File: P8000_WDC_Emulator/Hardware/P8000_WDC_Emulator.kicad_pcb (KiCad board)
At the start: 2 copper layers, 144 x 160.4 mm, 92 parts, among them Q1 CRYSTAL, SW1 SW_PUSH, X1 RS-232, X2 P8000, X3 SD-CON, X4 PATA, X5 4_Pin_Molex, X6 P8000-Compact, X7 AVR-ISP-6

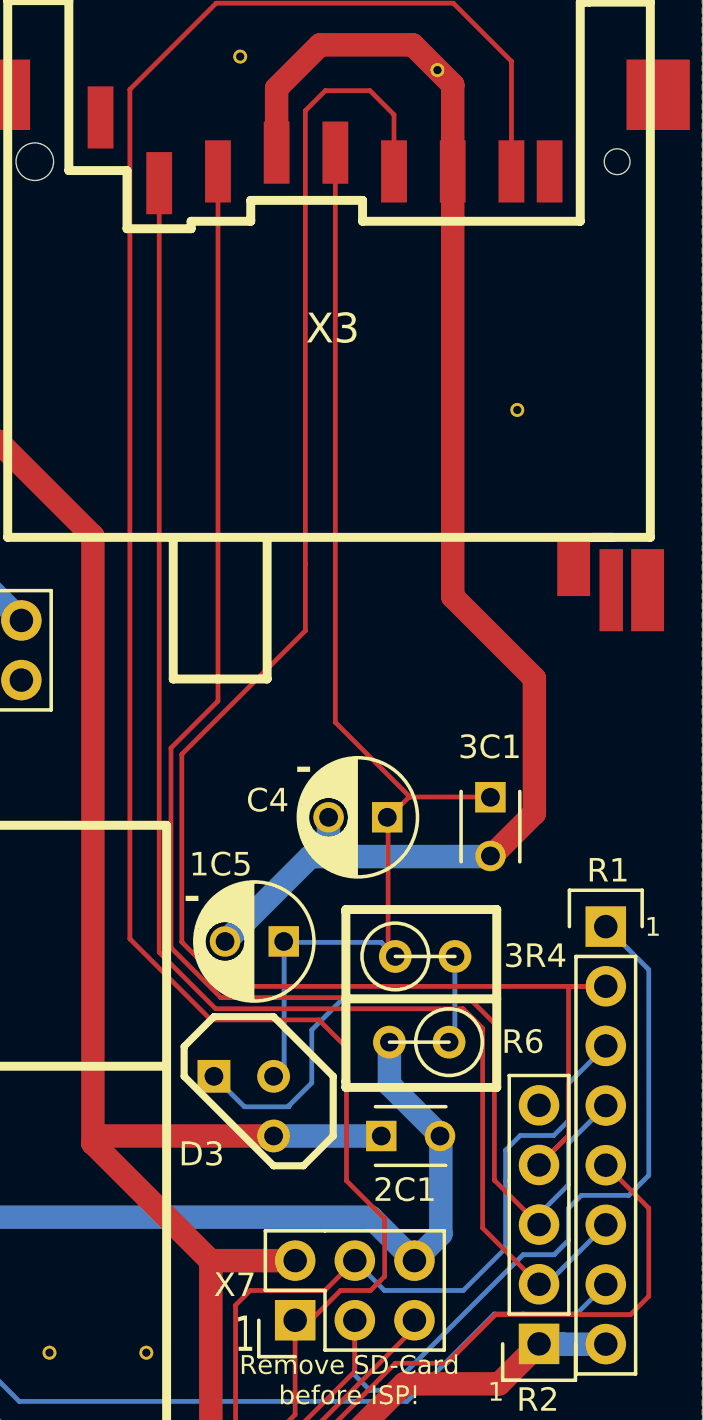
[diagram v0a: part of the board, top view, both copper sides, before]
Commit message: power line sizes for 3.3V
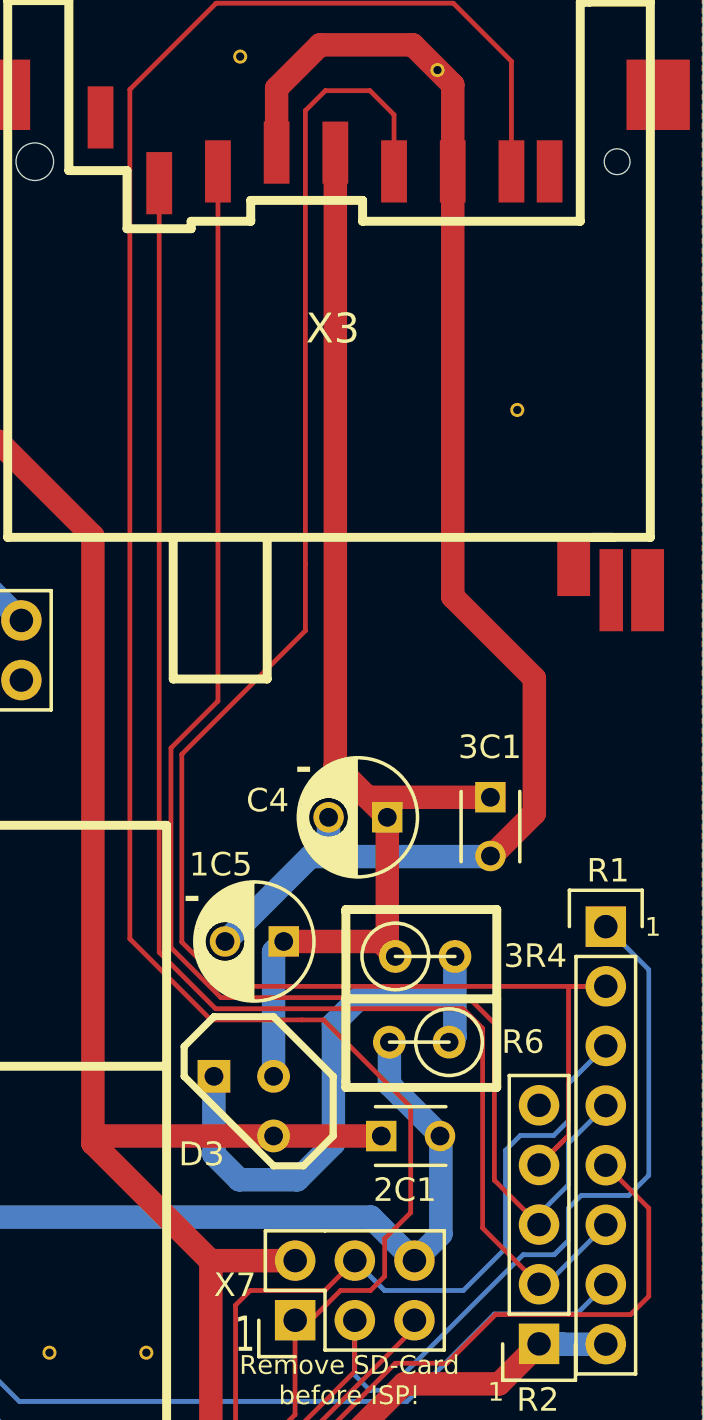
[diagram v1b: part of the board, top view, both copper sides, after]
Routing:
- net Net-(3R4-Pad2): track 17.8 -> 24.0 mm
- net +3V3: track 50.4 -> 53.4 mm
- net Net-(D1-Pad7): track 128.9 -> 129.9 mm
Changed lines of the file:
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@@
     (thickness 1.6002)
     (drawings 45)
-    (tracks 1224)
+    (tracks 1225)
     (zones 0)
     (modules 92)
@@
     (uvia_dia 0.508)
     (uvia_drill 0.127)
-    (add_net +3V3)
     (add_net //ASTB)
     (add_net //CS0)
@@
     (add_net "Net-(3C5-Pad1)")
     (add_net "Net-(3C5-Pad2)")
-    (add_net "Net-(3R4-Pad2)")
     (add_net "Net-(4C5-Pad2)")
     (add_net "Net-(5C5-Pad1)")
@@
     (uvia_dia 0.508)
     (uvia_drill 0.127)
+    (add_net +3V3)
     (add_net GND)
+    (add_net "Net-(3R4-Pad2)")
     (add_net VCC)
   )
@@
   (segment (start 146.32432 164.8206) (end 147.04568 164.09924) (width 1.00076) (layer Front) (net 41))
   (segment (start 146.32432 177.90414) (end 146.32432 164.8206) (width 1.00076) (layer Front) (net 41))
+  (segment (start 145.17116 74.39406) (end 149.75586 74.39406) (width 1.00076) (layer Front) (net 42))
+  (segment (start 149.75586 74.39406) (end 149.7584 74.3966) (width 1.00076) (layer Front) (net 42))
   (segment (start 149.75078 74.39406) (end 149.75586 74.39914) (width 1.00076) (layer Back) (net 42))
   (segment (start 66.04508 40.3606) (end 70.17512 36.23056) (width 1.00076) (layer Front) (net 42))
@@
   (segment (start 137.7823 74.39406) (end 137.47496 74.7014) (width 1.00076) (layer Front) (net 42))
   (segment (start 66.04508 41.28516) (end 75.77582 51.0159) (width 1.00076) (layer Front) (net 42))
-  (segment (start 145.17116 74.39406) (end 149.75078 74.39406) (width 1.00076) (layer Back) (net 42))
   (segment (start 75.77582 51.0159) (end 75.77582 59.25566) (width 1.00076) (layer Front) (net 42))
   (segment (start 145.17116 74.39406) (end 137.7823 74.39406) (width 1.00076) (layer Front) (net 42))
@@
   (segment (start 29.47416 115.12296) (end 29.47416 114.21364) (width 0.2032) (layer Back) (net 43))
   (segment (start 145.10004 95.60052) (end 152.67432 103.1748) (width 0.2032) (layer Front) (net 43))
-  (segment (start 150.04796 66.44132) (end 150.3553 66.74866) (width 0.2032) (layer Front) (net 44))
-  (segment (start 149.75586 66.14922) (end 150.3553 66.74866) (width 0.2032) (layer Back) (net 44))
-  (segment (start 145.62074 66.14922) (end 149.75586 66.14922) (width 0.2032) (layer Back) (net 44))
-  (segment (start 147.80006 32.51454) (end 147.80006 56.77662) (width 0.2032) (layer Front) (net 44))
-  (segment (start 147.80006 56.77662) (end 150.98014 59.9567) (width 0.2032) (layer Front) (net 44))
-  (segment (start 150.98014 59.9567) (end 150.94204 59.9567) (width 0.2032) (layer Front) (net 44))
-  (segment (start 150.94204 59.9567) (end 150.04796 60.85078) (width 0.2032) (layer Front) (net 44))
-  (segment (start 145.62074 71.40448) (end 145.17116 71.85406) (width 0.2032) (layer Back) (net 44))
-  (segment (start 145.62074 66.14922) (end 145.62074 71.40448) (width 0.2032) (layer Back) (net 44))
-  (segment (start 154.42946 59.9567) (end 150.98014 59.9567) (width 0.2032) (layer Front) (net 44))
-  (segment (start 150.04796 60.85078) (end 150.04796 66.44132) (width 0.2032) (layer Front) (net 44))
+  (segment (start 145.17116 71.85406) (end 145.17116 66.54292) (width 1.00076) (layer Back) (net 44))
+  (segment (start 145.17116 66.54292) (end 145.60296 66.11112) (width 1.00076) (layer Back) (net 44))
+  (segment (start 145.60296 66.11112) (end 149.71776 66.11112) (width 1.00076) (layer Front) (net 44))
+  (segment (start 149.71776 66.11112) (end 150.3553 66.74866) (width 1.00076) (layer Front) (net 44))
+  (segment (start 150.0124 60.82284) (end 150.0124 66.40576) (width 1.00076) (layer Front) (net 44))
+  (segment (start 150.0124 66.40576) (end 150.3553 66.74866) (width 1.00076) (layer Front) (net 44))
+  (segment (start 154.4066 59.9694) (end 149.15896 59.9694) (width 1.00076) (layer Front) (net 44))
+  (segment (start 149.15896 59.9694) (end 147.80006 58.6105) (width 1.00076) (layer Front) (net 44))
+  (segment (start 147.80006 32.51454) (end 147.80006 58.6105) (width 1.00076) (layer Front) (net 44))
+  (segment (start 147.80006 58.6105) (end 149.04 59.85044) (width 1.00076) (layer Front) (net 44))
+  (segment (start 149.04 59.85044) (end 150.0124 60.82284) (width 1.00076) (layer Front) (net 44))
   (segment (start 103.4 39.40048) (end 103.01224 39.40048) (width 0.2032) (layer Back) (net 45))
   (segment (start 103.01224 39.40048) (end 102.25272 40.16) (width 0.2032) (layer Back) (net 45))
@@
   (segment (start 30.06598 54.7497) (end 29.718 55.09768) (width 0.2032) (layer Back) (net 56))
   (segment (start 29.718 55.09768) (end 25.82672 55.09768) (width 0.2032) (layer Back) (net 56))
-  (segment (start 146.7993 72.12584) (end 146.7993 69.8754) (width 0.2032) (layer Back) (net 57))
-  (segment (start 152.8953 70.14718) (end 152.64384 70.39864) (width 0.2032) (layer Back) (net 57))
-  (segment (start 152.8953 68.60032) (end 151.74976 68.60032) (width 0.2032) (layer Back) (net 57))
-  (segment (start 145.82648 73.14946) (end 145.82648 73.09866) (width 0.2032) (layer Back) (net 57))
-  (segment (start 152.8953 66.74866) (end 152.8953 68.60032) (width 0.2032) (layer Back) (net 57))
-  (segment (start 148.07438 68.60032) (end 151.74976 68.60032) (width 0.2032) (layer Back) (net 57))
-  (segment (start 145.82648 73.09866) (end 146.7993 72.12584) (width 0.2032) (layer Back) (net 57))
-  (segment (start 143.92656 73.14946) (end 145.82648 73.14946) (width 0.2032) (layer Back) (net 57))
-  (segment (start 152.8953 68.60032) (end 152.8953 70.14718) (width 0.2032) (layer Back) (net 57))
-  (segment (start 146.7993 69.8754) (end 148.07438 68.60032) (width 0.2032) (layer Back) (net 57))
-  (segment (start 143.92656 73.14946) (end 142.63116 71.85406) (width 0.2032) (layer Back) (net 57))
+  (segment (start 152.8953 68.56) (end 148.78 68.56) (width 1.00076) (layer Back) (net 57))
+  (segment (start 142.63116 75.18116) (end 142.63116 71.85406) (width 1.00076) (layer Back) (net 57))
+  (segment (start 143.71 76.26) (end 142.63116 75.18116) (width 1.00076) (layer Back) (net 57))
+  (segment (start 146.18 76.26) (end 143.71 76.26) (width 1.00076) (layer Back) (net 57))
+  (segment (start 147.72 74.72) (end 146.18 76.26) (width 1.00076) (layer Back) (net 57))
+  (segment (start 147.72 69.62) (end 147.72 74.72) (width 1.00076) (layer Back) (net 57))
+  (segment (start 148.78 68.56) (end 147.72 69.62) (width 1.00076) (layer Back) (net 57))
+  (segment (start 152.8953 66.74866) (end 152.8953 68.56) (width 1.00076) (layer Back) (net 57))
+  (segment (start 152.8953 68.56) (end 152.8953 70.14718) (width 1.00076) (layer Back) (net 57))
+  (segment (start 152.8953 70.14718) (end 152.64384 70.39864) (width 1.00076) (layer Back) (net 57))
   (segment (start 30.06598 62.3697) (end 26.3144 66.12128) (width 0.2032) (layer Back) (net 58))
   (segment (start 26.3144 66.12128) (end 25.84958 66.12128) (width 0.2032) (layer Back) (net 58))
@@
   (segment (start 155.6766 74.37374) (end 155.04922 75.00112) (width 0.2032) (layer Back) (net 61))
   (segment (start 157.10154 74.37374) (end 155.6766 74.37374) (width 0.2032) (layer Back) (net 61))
-  (segment (start 148.27504 70.6247) (end 148.27504 76.3016) (width 0.2032) (layer Front) (net 62))
-  (segment (start 147.10156 69.45122) (end 148.27504 70.6247) (width 0.2032) (layer Front) (net 62))
-  (segment (start 142.50162 69.45122) (end 147.10156 69.45122) (width 0.2032) (layer Front) (net 62))
+  (segment (start 146.38 69.45122) (end 147.30122 69.45122) (width 0.2032) (layer Front) (net 62))
+  (segment (start 151.01 77.66) (end 149.90064 78.76936) (width 0.2032) (layer Front) (net 62))
+  (segment (start 151.01 73.16) (end 151.01 77.66) (width 0.2032) (layer Front) (net 62))
+  (segment (start 147.30122 69.45122) (end 151.01 73.16) (width 0.2032) (layer Front) (net 62))
+  (segment (start 142.50162 69.45122) (end 146.38 69.45122) (width 0.2032) (layer Front) (net 62))
   (segment (start 148.02358 80.9752) (end 146.75358 82.2452) (width 0.2032) (layer Front) (net 62))
   (segment (start 149.29866 80.9752) (end 148.02358 80.9752) (width 0.2032) (layer Front) (net 62))
   (segment (start 149.90064 80.37322) (end 149.29866 80.9752) (width 0.2032) (layer Front) (net 62))
-  (segment (start 149.90064 77.9272) (end 149.90064 80.37322) (width 0.2032) (layer Front) (net 62))
-  (segment (start 148.27504 76.3016) (end 149.90064 77.9272) (width 0.2032) (layer Front) (net 62))
+  (segment (start 149.90064 78.76936) (end 149.90064 80.37322) (width 0.2032) (layer Front) (net 62))
   (segment (start 144.05102 92.49918) (end 144.05102 95.9993) (width 0.2032) (layer Front) (net 62))
   (segment (start 151.6761 112.9411) (end 145.7452 118.872) (width 0.2032) (layer Front) (net 62))

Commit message: begin work on v2.1
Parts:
- removed 1C5: 1u, Capacitors_ThroughHole:C_Radial_D5_L6_P2.5
- removed 1D5, 2D5: 74HCT245, Housings_DIP:DIP-20_W7.62mm
- removed 1R5, 2R5: 4k7, Pin_Headers:Pin_Header_Straight_1x05
- removed 3R4: 220, Discret:R1
- removed C4: 47u, Capacitors_ThroughHole:C_Radial_D5_L6_P2.5
- removed R6: 330, Discret:R1
- added 1C3: 100u, Capacitors_ThroughHole:C_Radial_D5_L6_P2.5, F.Cu at (199.1, 82.6)
- added 1C4: 1u, Capacitors_ThroughHole:C_Radial_D5_L6_P2.5, F.Cu at (3.75, 40.0)
- added 2C3: 100u, Capacitors_ThroughHole:C_Radial_D5_L6_P2.5, F.Cu at (213.1, 82.0)
- added 2C4: 1u, Capacitors_ThroughHole:C_Radial_D5_L6_P2.5, F.Cu at (-17.2, 41.4)
- added 3C4: 1u, Capacitors_ThroughHole:C_Radial_D5_L6_P2.5, F.Cu at (-6.99, 44.3)
- added 4C4: 1u, Capacitors_ThroughHole:C_Radial_D5_L6_P2.5, F.Cu at (-31.1, 44.7)
- added 7C1: 100n, Capacitors_ThroughHole:C_Disc_D3_P2.5, F.Cu at (175.8, 146.8)
- added 8C1: 100n, Capacitors_ThroughHole:C_Disc_D3_P2.5, F.Cu at (171.0, 139.5)
- added C2: 470u, Capacitors_ThroughHole:C_Radial_D5_L6_P2.5, F.Cu at (3.68, 27.8)
- added D5: 74HCT245, Housings_DIP:DIP-20_W7.62mm, F.Cu at (97.2, 33.7)
- added D6: 74HCT243, Housings_DIP:DIP-14_W7.62mm, F.Cu at (125.0, 42.0)
- added D7: 74HCT573, Housings_DIP:DIP-20_W7.62mm, F.Cu at (128.7, 31.8)
- D3: value LM317 -> TS1117 BCW33; footprint TO92-LM317 -> TO_SOT_Packages_SMD:SOT-223
- D4: value 74HCT03 -> 74HCT00
- moved D3 89.3 mm to (233.2, 73.6), turned to 0 degrees
- moved 2C1 50.9 mm to (200.2, 67.8)
- moved 3C1 45.8 mm to (200.1, 63.5), turned to 0 degrees
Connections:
- D1 pad 19: Net-(2R5-Pad2) -> Net-(D1-Pad19)
- D2 pad 1: Net-(3C5-Pad1) -> Net-(3C4-Pad1)
- D2 pad 2: Net-(5C5-Pad1) -> Net-(1C4-Pad1)
- D2 pad 3: Net-(3C5-Pad2) -> Net-(3C4-Pad2)
- D2 pad 4: Net-(2C5-Pad1) -> Net-(2C4-Pad1)
- D2 pad 5: Net-(2C5-Pad2) -> Net-(2C4-Pad2)
- D2 pad 6: Net-(4C5-Pad2) -> Net-(4C4-Pad2)
- D3 pad 1: Net-(3R4-Pad2) -> GND
- D4 pad 12: Net-(1R5-Pad5) -> VCC
- D4 pad 13: Net-(1R5-Pad5) -> VCC
- JP1 pad 1: Net-(2R5-Pad2) -> Net-(D1-Pad19)
- R2 pad 5: Net-(R2-Pad5) -> Net-(D1-Pad19)
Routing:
- net Net-(2R5-Pad2): track 168.0 -> 0.00 mm
- net Net-(D1-Pad18): track 156.3 -> 0.33 mm, vias 1 -> 0
- net Net-(D1-Pad19): track 0.00 -> 135.9 mm
- net //RST2: track 111.8 -> 0.00 mm
- net Net-(D4-Pad8): track 102.2 -> 10.2 mm
- net VCC: track 416.6 -> 325.2 mm
- net //TE: track 81.2 -> 0.00 mm, vias 1 -> 0
- net GND: track 612.5 -> 534.9 mm
- net /PC5: track 139.2 -> 210.4 mm
- net Net-(1R5-Pad5): track 68.4 -> 0.00 mm
- net /PC0: track 210.9 -> 145.9 mm, vias 2 -> 1
- net /RST: track 57.4 -> 0.00 mm, vias 1 -> 0
- net +3V3: track 53.4 -> 0.00 mm
- net //TR: track 76.1 -> 25.7 mm
- net /PC1: track 212.8 -> 172.1 mm, vias 1 -> 0
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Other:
- board text added: "P8000 WDC Emulator v 2.1 (c) Oliver Lehmann 2012, 2013, 2015, 2016 lehmann@ans-netz.de"
- board text removed: "P8000 WDC Emulator v 2.0 (c) Oliver Lehmann 2012, 2013, 2015, 2016 lehmann@ans-netz.de"

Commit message: version 2.1
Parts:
- removed 2C5, 3C5, 4C5, 5C5, 6C5: 1u, Capacitors_ThroughHole:C_Radial_D5_L6_P2.5
- removed the VIA-0.6mm at (120.6, 112.9)
- removed the VIA-0.6mm at (102.7, 67.2)
- removed the VIA-0.6mm at (109.4, 78.5)
- removed the VIA-0.6mm at (76.8, 90.7)
- removed the VIA-0.6mm at (79.9, 117.2)
- removed the VIA-0.6mm at (154.0, 150.4)
- removed the VIA-0.6mm at (157.6, 119.1)
- removed the VIA-0.6mm at (47.9, 54.5)
- removed the VIA-0.6mm at (68.0, 47.8)
- removed the VIA-0.6mm at (77.7, 44.2)
- removed the VIA-0.6mm at (155.5, 43.5)
- removed the VIA-0.6mm at (122.2, 87.7)
- removed the VIA-0.6mm at (152.2, 29.0)
- removed the VIA-0.6mm at (143.7, 28.4)
- removed the VIA-0.6mm at (109.8, 60.4)
- removed the VIA-0.6mm at (112.5, 62.8)
- removed the VIA-0.6mm at (102.2, 85.9)
- removed the VIA-0.6mm at (107.6, 112.9)
- removed the VIA-0.6mm at (139.8, 83.6)
- removed the VIA-0.6mm at (139.0, 88.2)
- removed the VIA-0.6mm at (135.6, 83.6)
- removed the VIA-0.6mm at (152.5, 124.2)
- removed the VIA-0.6mm at (122.1, 101.8)
- removed the VIA-0.6mm at (151.2, 150.4)
- removed the VIA-0.6mm at (123.2, 134.9)
- removed the VIA-0.6mm at (129.0, 120.8)
- removed the VIA-0.6mm at (135.4, 127.1)
- removed the VIA-0.6mm at (89.3, 143.1)
- removed the VIA-0.6mm at (46.2, 142.5)
- removed the VIA-0.6mm at (123.4, 172.0)
- removed the VIA-0.6mm at (89.2, 171.1)
- removed the VIA-0.6mm at (46.8, 171.3)
- removed the VIA-0.6mm at (47.2, 129.3)
- removed the VIA-0.6mm at (127.8, 107.3)
- removed the VIA-0.6mm at (49.2, 96.3)
- removed the VIA-0.6mm at (49.1, 75.6)
- removed the VIA-0.6mm at (128.0, 93.2)
- removed the VIA-0.6mm at (117.4, 86.7)
- removed the VIA-0.6mm at (117.4, 82.2)
- removed the VIA-0.6mm at (112.2, 81.5)
- removed the VIA-0.6mm at (108.1, 73.0)
- added VIA-0.6mm: VAL**, Footprints:VIA-0.6mm, F.Cu at (161.0, 103.3)
- added VIA-0.6mm: VAL**, Footprints:VIA-0.6mm, F.Cu at (76.8, 92.1)
- added VIA-0.6mm: VAL**, Footprints:VIA-0.6mm, F.Cu at (86.4, 128.3)
- added VIA-0.6mm: VAL**, Footprints:VIA-0.6mm, F.Cu at (89.5, 128.3)
- added VIA-0.6mm: VAL**, Footprints:VIA-0.6mm, F.Cu at (92.7, 128.3)
- added VIA-0.6mm: VAL**, Footprints:VIA-0.6mm, F.Cu at (83.2, 128.3)
- added VIA-0.6mm: VAL**, Footprints:VIA-0.6mm, F.Cu at (80.0, 128.3)
- added VIA-0.6mm: VAL**, Footprints:VIA-0.6mm, F.Cu at (76.8, 128.3)
- added VIA-0.6mm: VAL**, Footprints:VIA-0.6mm, F.Cu at (95.9, 148.0)
- added VIA-0.6mm: VAL**, Footprints:VIA-0.6mm, F.Cu at (99.1, 148.0)
- added VIA-0.6mm: VAL**, Footprints:VIA-0.6mm, F.Cu at (102.2, 148.0)
- added VIA-0.6mm: VAL**, Footprints:VIA-0.6mm, F.Cu at (111.8, 148.0)
- added VIA-0.6mm: VAL**, Footprints:VIA-0.6mm, F.Cu at (80.0, 92.1)
- added VIA-0.6mm: VAL**, Footprints:VIA-0.6mm, F.Cu at (108.6, 148.0)
- added VIA-0.6mm: VAL**, Footprints:VIA-0.6mm, F.Cu at (105.4, 148.0)
- added VIA-0.6mm: VAL**, Footprints:VIA-0.6mm, F.Cu at (86.4, 148.0)
- added VIA-0.6mm: VAL**, Footprints:VIA-0.6mm, F.Cu at (89.5, 148.0)
- added VIA-0.6mm: VAL**, Footprints:VIA-0.6mm, F.Cu at (92.7, 148.0)
- added VIA-0.6mm: VAL**, Footprints:VIA-0.6mm, F.Cu at (83.2, 148.0)
- added VIA-0.6mm: VAL**, Footprints:VIA-0.6mm, F.Cu at (80.0, 148.0)
- added VIA-0.6mm: VAL**, Footprints:VIA-0.6mm, F.Cu at (76.8, 148.0)
- added VIA-0.6mm: VAL**, Footprints:VIA-0.6mm, F.Cu at (95.9, 155.6)
- added VIA-0.6mm: VAL**, Footprints:VIA-0.6mm, F.Cu at (99.1, 155.6)
- added VIA-0.6mm: VAL**, Footprints:VIA-0.6mm, F.Cu at (83.2, 92.1)
- added VIA-0.6mm: VAL**, Footprints:VIA-0.6mm, F.Cu at (102.2, 155.6)
- added VIA-0.6mm: VAL**, Footprints:VIA-0.6mm, F.Cu at (111.8, 155.6)
- added VIA-0.6mm: VAL**, Footprints:VIA-0.6mm, F.Cu at (108.6, 155.6)
- added VIA-0.6mm: VAL**, Footprints:VIA-0.6mm, F.Cu at (105.4, 155.6)
- added VIA-0.6mm: VAL**, Footprints:VIA-0.6mm, F.Cu at (86.4, 155.6)
- added VIA-0.6mm: VAL**, Footprints:VIA-0.6mm, F.Cu at (89.5, 155.6)
- added VIA-0.6mm: VAL**, Footprints:VIA-0.6mm, F.Cu at (92.7, 155.6)
- added VIA-0.6mm: VAL**, Footprints:VIA-0.6mm, F.Cu at (83.2, 155.6)
- added VIA-0.6mm: VAL**, Footprints:VIA-0.6mm, F.Cu at (80.0, 155.6)
- added VIA-0.6mm: VAL**, Footprints:VIA-0.6mm, F.Cu at (76.8, 155.6)
- added VIA-0.6mm: VAL**, Footprints:VIA-0.6mm, F.Cu at (92.7, 92.1)
- added VIA-0.6mm: VAL**, Footprints:VIA-0.6mm, F.Cu at (96.5, 174.6)
- added VIA-0.6mm: VAL**, Footprints:VIA-0.6mm, F.Cu at (99.7, 174.6)
- added VIA-0.6mm: VAL**, Footprints:VIA-0.6mm, F.Cu at (102.9, 174.6)
- added VIA-0.6mm: VAL**, Footprints:VIA-0.6mm, F.Cu at (112.4, 174.6)
- added VIA-0.6mm: VAL**, Footprints:VIA-0.6mm, F.Cu at (109.2, 174.6)
- added VIA-0.6mm: VAL**, Footprints:VIA-0.6mm, F.Cu at (106.0, 174.6)
- added VIA-0.6mm: VAL**, Footprints:VIA-0.6mm, F.Cu at (87.0, 174.6)
- added VIA-0.6mm: VAL**, Footprints:VIA-0.6mm, F.Cu at (90.2, 174.6)
- added VIA-0.6mm: VAL**, Footprints:VIA-0.6mm, F.Cu at (93.3, 174.6)
- added VIA-0.6mm: VAL**, Footprints:VIA-0.6mm, F.Cu at (83.8, 174.6)
- added VIA-0.6mm: VAL**, Footprints:VIA-0.6mm, F.Cu at (89.5, 92.1)
- added VIA-0.6mm: VAL**, Footprints:VIA-0.6mm, F.Cu at (80.6, 174.6)
- added VIA-0.6mm: VAL**, Footprints:VIA-0.6mm, F.Cu at (77.5, 174.6)
- added VIA-0.6mm: VAL**, Footprints:VIA-0.6mm, F.Cu at (157.5, 156.2)
- added VIA-0.6mm: VAL**, Footprints:VIA-0.6mm, F.Cu at (154.3, 156.2)
- added VIA-0.6mm: VAL**, Footprints:VIA-0.6mm, F.Cu at (151.1, 156.2)
- added VIA-0.6mm: VAL**, Footprints:VIA-0.6mm, F.Cu at (158.8, 163.2)
- added VIA-0.6mm: VAL**, Footprints:VIA-0.6mm, F.Cu at (155.6, 163.2)
- added VIA-0.6mm: VAL**, Footprints:VIA-0.6mm, F.Cu at (23.5, 104.1)
- added VIA-0.6mm: VAL**, Footprints:VIA-0.6mm, F.Cu at (42.5, 99.1)
- added VIA-0.6mm: VAL**, Footprints:VIA-0.6mm, F.Cu at (52.1, 99.1)
- added VIA-0.6mm: VAL**, Footprints:VIA-0.6mm, F.Cu at (86.4, 92.1)
- added VIA-0.6mm: VAL**, Footprints:VIA-0.6mm, F.Cu at (48.9, 99.1)
- added VIA-0.6mm: VAL**, Footprints:VIA-0.6mm, F.Cu at (45.7, 99.1)
- added VIA-0.6mm: VAL**, Footprints:VIA-0.6mm, F.Cu at (46.4, 80.0)
- added VIA-0.6mm: VAL**, Footprints:VIA-0.6mm, F.Cu at (43.2, 80.0)
- added VIA-0.6mm: VAL**, Footprints:VIA-0.6mm, F.Cu at (40.0, 80.0)
- added VIA-0.6mm: VAL**, Footprints:VIA-0.6mm, F.Cu at (44.5, 53.3)
- added VIA-0.6mm: VAL**, Footprints:VIA-0.6mm, F.Cu at (41.3, 53.3)
- added VIA-0.6mm: VAL**, Footprints:VIA-0.6mm, F.Cu at (44.5, 59.1)
- added VIA-0.6mm: VAL**, Footprints:VIA-0.6mm, F.Cu at (41.3, 59.1)
- added VIA-0.6mm: VAL**, Footprints:VIA-0.6mm, F.Cu at (32.7, 60.6)
- added VIA-0.6mm: VAL**, Footprints:VIA-0.6mm, F.Cu at (105.4, 92.1)
- added VIA-0.6mm: VAL**, Footprints:VIA-0.6mm, F.Cu at (32.7, 63.8)
- added VIA-0.6mm: VAL**, Footprints:VIA-0.6mm, F.Cu at (34.6, 51.1)
- added VIA-0.6mm: VAL**, Footprints:VIA-0.6mm, F.Cu at (34.6, 54.3)
- added VIA-0.6mm: VAL**, Footprints:VIA-0.6mm, F.Cu at (74.0, 35.4)
- added VIA-0.6mm: VAL**, Footprints:VIA-0.6mm, F.Cu at (108.6, 92.1)
- added VIA-0.6mm: VAL**, Footprints:VIA-0.6mm, F.Cu at (111.8, 92.1)
- added VIA-0.6mm: VAL**, Footprints:VIA-0.6mm, F.Cu at (102.2, 92.1)
- added VIA-0.6mm: VAL**, Footprints:VIA-0.6mm, F.Cu at (157.8, 103.3)
- added VIA-0.6mm: VAL**, Footprints:VIA-0.6mm, F.Cu at (99.1, 92.1)
- added VIA-0.6mm: VAL**, Footprints:VIA-0.6mm, F.Cu at (95.9, 92.1)
- added VIA-0.6mm: VAL**, Footprints:VIA-0.6mm, F.Cu at (76.8, 84.5)
- added VIA-0.6mm: VAL**, Footprints:VIA-0.6mm, F.Cu at (80.0, 84.5)
- added VIA-0.6mm: VAL**, Footprints:VIA-0.6mm, F.Cu at (83.2, 84.5)
- added VIA-0.6mm: VAL**, Footprints:VIA-0.6mm, F.Cu at (92.7, 84.5)
- added VIA-0.6mm: VAL**, Footprints:VIA-0.6mm, F.Cu at (89.5, 84.5)
- added VIA-0.6mm: VAL**, Footprints:VIA-0.6mm, F.Cu at (86.4, 84.5)
- added VIA-0.6mm: VAL**, Footprints:VIA-0.6mm, F.Cu at (105.4, 84.5)
- added VIA-0.6mm: VAL**, Footprints:VIA-0.6mm, F.Cu at (108.6, 84.5)
- added VIA-0.6mm: VAL**, Footprints:VIA-0.6mm, F.Cu at (103.1, 61.8)
- added VIA-0.6mm: VAL**, Footprints:VIA-0.6mm, F.Cu at (111.8, 84.5)
- added VIA-0.6mm: VAL**, Footprints:VIA-0.6mm, F.Cu at (102.2, 84.5)
- added VIA-0.6mm: VAL**, Footprints:VIA-0.6mm, F.Cu at (99.1, 84.5)
- added VIA-0.6mm: VAL**, Footprints:VIA-0.6mm, F.Cu at (95.9, 84.5)
- added VIA-0.6mm: VAL**, Footprints:VIA-0.6mm, F.Cu at (121.3, 24.8)
- added VIA-0.6mm: VAL**, Footprints:VIA-0.6mm, F.Cu at (121.3, 27.3)
- added VIA-0.6mm: VAL**, Footprints:VIA-0.6mm, F.Cu at (124.6, 27.3)
- added VIA-0.6mm: VAL**, Footprints:VIA-0.6mm, F.Cu at (127.6, 27.3)
- added VIA-0.6mm: VAL**, Footprints:VIA-0.6mm, F.Cu at (127.6, 24.8)
- added VIA-0.6mm: VAL**, Footprints:VIA-0.6mm, F.Cu at (130.8, 27.3)
- added VIA-0.6mm: VAL**, Footprints:VIA-0.6mm, F.Cu at (80.0, 64.8)
- added VIA-0.6mm: VAL**, Footprints:VIA-0.6mm, F.Cu at (134.0, 27.3)
- added VIA-0.6mm: VAL**, Footprints:VIA-0.6mm, F.Cu at (137.2, 27.3)
- added VIA-0.6mm: VAL**, Footprints:VIA-0.6mm, F.Cu at (137.2, 24.8)
- added VIA-0.6mm: VAL**, Footprints:VIA-0.6mm, F.Cu at (134.0, 24.8)
- added VIA-0.6mm: VAL**, Footprints:VIA-0.6mm, F.Cu at (130.8, 24.8)
- added VIA-0.6mm: VAL**, Footprints:VIA-0.6mm, F.Cu at (130.8, 29.8)
- added VIA-0.6mm: VAL**, Footprints:VIA-0.6mm, F.Cu at (134.0, 29.8)
- added VIA-0.6mm: VAL**, Footprints:VIA-0.6mm, F.Cu at (137.2, 29.8)
- added VIA-0.6mm: VAL**, Footprints:VIA-0.6mm, F.Cu at (139.4, 137.5)
- added VIA-0.6mm: VAL**, Footprints:VIA-0.6mm, F.Cu at (137.4, 128.3)
- added VIA-0.6mm: VAL**, Footprints:VIA-0.6mm, F.Cu at (83.2, 64.8)
- added VIA-0.6mm: VAL**, Footprints:VIA-0.6mm, F.Cu at (134.2, 128.3)
- added VIA-0.6mm: VAL**, Footprints:VIA-0.6mm, F.Cu at (129.5, 106.9)
- added VIA-0.6mm: VAL**, Footprints:VIA-0.6mm, F.Cu at (129.5, 114.6)
- added VIA-0.6mm: VAL**, Footprints:VIA-0.6mm, F.Cu at (75.8, 38.2)
- added VIA-0.6mm: VAL**, Footprints:VIA-0.6mm, F.Cu at (142.9, 26.7)
- added VIA-0.6mm: VAL**, Footprints:VIA-0.6mm, F.Cu at (142.9, 28.6)
- added VIA-0.6mm: VAL**, Footprints:VIA-0.6mm, F.Cu at (142.9, 24.8)
- added VIA-0.6mm: VAL**, Footprints:VIA-0.6mm, F.Cu at (150.5, 24.8)
- added VIA-0.6mm: VAL**, Footprints:VIA-0.6mm, F.Cu at (151.8, 26.7)
- added VIA-0.6mm: VAL**, Footprints:VIA-0.6mm, F.Cu at (153.0, 28.6)
- added VIA-0.6mm: VAL**, Footprints:VIA-0.6mm, F.Cu at (86.4, 64.8)
- added VIA-0.6mm: VAL**, Footprints:VIA-0.6mm, F.Cu at (155.6, 45.1)
- added VIA-0.6mm: VAL**, Footprints:VIA-0.6mm, F.Cu at (152.4, 45.1)
- added VIA-0.6mm: VAL**, Footprints:VIA-0.6mm, F.Cu at (149.2, 45.1)
- added VIA-0.6mm: VAL**, Footprints:VIA-0.6mm, F.Cu at (135.3, 58.4)
- added VIA-0.6mm: VAL**, Footprints:VIA-0.6mm, F.Cu at (132.1, 58.4)
- added VIA-0.6mm: VAL**, Footprints:VIA-0.6mm, F.Cu at (128.9, 58.4)
- added VIA-0.6mm: VAL**, Footprints:VIA-0.6mm, F.Cu at (22.2, 41.3)
- added VIA-0.6mm: VAL**, Footprints:VIA-0.6mm, F.Cu at (34.9, 40.0)
- added VIA-0.6mm: VAL**, Footprints:VIA-0.6mm, F.Cu at (38.1, 40.0)
- added VIA-0.6mm: VAL**, Footprints:VIA-0.6mm, F.Cu at (22.2, 44.5)
- added VIA-0.6mm: VAL**, Footprints:VIA-0.6mm, F.Cu at (95.9, 64.8)
- added VIA-0.6mm: VAL**, Footprints:VIA-0.6mm, F.Cu at (95.9, 106.7)
- added VIA-0.6mm: VAL**, Footprints:VIA-0.6mm, F.Cu at (99.1, 106.7)
- added VIA-0.6mm: VAL**, Footprints:VIA-0.6mm, F.Cu at (102.2, 106.7)
- added VIA-0.6mm: VAL**, Footprints:VIA-0.6mm, F.Cu at (111.8, 106.7)
- added VIA-0.6mm: VAL**, Footprints:VIA-0.6mm, F.Cu at (108.6, 106.7)
- added VIA-0.6mm: VAL**, Footprints:VIA-0.6mm, F.Cu at (105.4, 106.7)
- added VIA-0.6mm: VAL**, Footprints:VIA-0.6mm, F.Cu at (86.4, 106.7)
- added VIA-0.6mm: VAL**, Footprints:VIA-0.6mm, F.Cu at (89.5, 106.7)
- added VIA-0.6mm: VAL**, Footprints:VIA-0.6mm, F.Cu at (92.7, 106.7)
- added VIA-0.6mm: VAL**, Footprints:VIA-0.6mm, F.Cu at (83.2, 106.7)
- added VIA-0.6mm: VAL**, Footprints:VIA-0.6mm, F.Cu at (92.7, 64.8)
- added VIA-0.6mm: VAL**, Footprints:VIA-0.6mm, F.Cu at (80.0, 106.7)
- added VIA-0.6mm: VAL**, Footprints:VIA-0.6mm, F.Cu at (76.8, 106.7)
- added VIA-0.6mm: VAL**, Footprints:VIA-0.6mm, F.Cu at (95.9, 114.3)
- added VIA-0.6mm: VAL**, Footprints:VIA-0.6mm, F.Cu at (99.1, 114.3)
- added VIA-0.6mm: VAL**, Footprints:VIA-0.6mm, F.Cu at (102.2, 114.3)
- added VIA-0.6mm: VAL**, Footprints:VIA-0.6mm, F.Cu at (111.8, 114.3)
- added VIA-0.6mm: VAL**, Footprints:VIA-0.6mm, F.Cu at (108.6, 114.3)
- added VIA-0.6mm: VAL**, Footprints:VIA-0.6mm, F.Cu at (105.4, 114.3)
- added VIA-0.6mm: VAL**, Footprints:VIA-0.6mm, F.Cu at (86.4, 114.3)
- added VIA-0.6mm: VAL**, Footprints:VIA-0.6mm, F.Cu at (89.5, 114.3)
- added VIA-0.6mm: VAL**, Footprints:VIA-0.6mm, F.Cu at (89.5, 64.8)
- added VIA-0.6mm: VAL**, Footprints:VIA-0.6mm, F.Cu at (92.7, 114.3)
- added VIA-0.6mm: VAL**, Footprints:VIA-0.6mm, F.Cu at (83.2, 114.3)
- added VIA-0.6mm: VAL**, Footprints:VIA-0.6mm, F.Cu at (80.0, 114.3)
- added VIA-0.6mm: VAL**, Footprints:VIA-0.6mm, F.Cu at (76.8, 114.3)
- added VIA-0.6mm: VAL**, Footprints:VIA-0.6mm, F.Cu at (95.9, 128.3)
- added VIA-0.6mm: VAL**, Footprints:VIA-0.6mm, F.Cu at (99.1, 128.3)
- added VIA-0.6mm: VAL**, Footprints:VIA-0.6mm, F.Cu at (102.2, 128.3)
- added VIA-0.6mm: VAL**, Footprints:VIA-0.6mm, F.Cu at (111.8, 128.3)
- added VIA-0.6mm: VAL**, Footprints:VIA-0.6mm, F.Cu at (108.6, 128.3)
- added VIA-0.6mm: VAL**, Footprints:VIA-0.6mm, F.Cu at (105.4, 128.3)
- C2: footprint Capacitors_ThroughHole:C_Radial_D5_L6_P2.5 -> Capacitors_ThroughHole:C_Radial_D8_L13_P3.8
- D3: footprint TO_SOT_Packages_SMD:SOT-223 -> Footprints:SOT-223
- Hole-Outer-1, Hole-Outer-2, Hole-Outer-3, Hole-Outer-4: footprint HOLE_4x8mm_pad -> Footprints:HOLE_4x8mm_pad
- moved X7 143.2 mm to (25.4, 159.4)
- moved D3 117.9 mm to (124.5, 27.9)
- moved 2C3 100.6 mm to (123.2, 36.8), turned to 180 degrees
- moved 6C1 96.7 mm to (147.3, 62.2), turned to 180 degrees
- moved 7C1 86.2 mm to (158.8, 62.2), turned to 180 degrees
- moved 1C3 85.4 mm to (127.0, 36.8)
- moved D4 82.8 mm to (142.2, 66.0), turned to 0 degrees
- moved 3C1 79.9 mm to (123.2, 41.9), turned to 180 degrees
- moved 2C1 77.7 mm to (127.0, 41.9)
- moved R2 60.5 mm to (111.8, 42.5), turned to 270 degrees
- moved 4C4 60.0 mm to (25.9, 63.6), turned to 270 degrees
- moved D7 59.0 mm to (69.8, 35.6)
- moved R1 58.8 mm to (116.8, 24.8)
- moved 2C4 46.2 mm to (25.9, 58.0), turned to 270 degrees
- moved D6 37.4 mm to (153.7, 66.0), turned to 0 degrees
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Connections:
- D4 pad 12: VCC -> Net-(D1-Pad18)
- D4 pad 13: VCC -> Net-(D1-Pad18)
- D7 pad 1: VCC -> GND
- D7 pad 11: Net-(D1-Pad18) -> Net-(D4-Pad11)
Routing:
- net VCC: track 325.2 -> 616.7 mm, vias 1 -> 0
- net Net-(D1-Pad18): track 0.33 -> 269.6 mm, vias 0 -> 3
- net Net-(D1-Pad8): track 77.7 -> 301.4 mm, vias 0 -> 1
- net Net-(D1-Pad7): track 129.9 -> 341.1 mm, vias 0 -> 2
- net Net-(D1-Pad6): track 64.9 -> 274.4 mm, vias 0 -> 1
- net //TE: track 0.00 -> 132.2 mm
- net Net-(D4-Pad11): track 0.00 -> 123.2 mm, vias 0 -> 1
- net //RST2: track 0.00 -> 113.0 mm
- net /PC4: track 117.8 -> 222.0 mm, vias 1 -> 0
- net /PC3: track 120.6 -> 216.5 mm, vias 1 -> 0
- net //TR: track 25.7 -> 113.0 mm
- net /PC0: track 145.9 -> 233.0 mm, vias 1 -> 0
- net /PC2: track 127.4 -> 212.2 mm, vias 1 -> 0
- net GND: track 534.9 -> 612.0 mm, vias 1 -> 2
- net +3V3: track 0.00 -> 62.4 mm
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- added copper zone on B.Cu, net +3V3
- added copper zone on F.Cu, net +3V3
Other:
- board text removed: "Remove SD-Card before ISP!"
